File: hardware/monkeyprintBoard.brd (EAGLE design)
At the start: 65 x 55.9 mm, 46 parts, among them Q1 BSS123

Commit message: Updated eagle files.
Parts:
- removed GPIO: (no value), connectors:X10N-DIL
- removed H1, H2, H3, H4: MOUNT-HOLE3.0, holes:3,0
- added ARDUINO_PRO_MICRO: ARDUINOPROMICRO, arduinoProMicro:ARDUINOPROMICRO
- added C7: 100n, rcl:C0603
- added R15: 220R, rcl:R0603
- added R17: 10k, rcl:R0603
- added R19: 0R, rcl:R0603
- added X3: (no value), connectors:X02N-SIL
- U$1: value ARDUINOPROMICRO -> MONKEYPRINTPICONNECTOR; device arduinoProMicro:ARDUINOPROMICRO -> monkeyprintPiConnector:MONKEYPRINTPICONNECTOR
- moved U$1 35.9 mm to (51.6, 3.49)
- moved R8 9.67 mm to (25.4, 48.3), turned to 90 degrees
- moved R10 8.28 mm to (33.0, 48.3), turned to 90 degrees
- moved R12 8.28 mm to (31.1, 48.3), turned to 90 degrees
- moved C4 4.58 mm to (54.0, 9.53)
- moved R5 4.26 mm to (47.0, 31.8), turned to 0 degrees
- moved R2 3.70 mm to (44.5, 31.1)
- moved D1 2.54 mm to (20.3, 52.7)
- moved LEDS 1.91 mm to (61.6, 38.7)
- moved R9 1.42 mm to (48.3, 36.8)
- moved X1 1.35 mm to (18.7, 39.7)
- moved R13 1.27 mm to (59.1, 38.7)
- moved R6 0.90 mm to (53.3, 23.5)
- moved R7 0.90 mm to (55.2, 23.5)
- moved Q1 0.63 mm to (54.0, 20.3)
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- renumbered U$2 to POLOLU_DRV8825_BUILD, U$3 to POLOLU_DRV8825_TILT
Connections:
- new net N$49: R17.1, R19.2, U$6.6
- new net N$50: ARDUINO_PRO_MICRO.14, C7.1, R19.1
- net GND: now also ARDUINO_PRO_MICRO.23, ARDUINO_PRO_MICRO.3, ARDUINO_PRO_MICRO.4, C7.2, U$1.GND1, U$1.GND2, X3.2; no longer GPIO.6, GPIO.9, U$1.23, U$1.3, U$1.4
- net N$1: now also ARDUINO_PRO_MICRO.7; no longer U$1.7
- net N$12: now also ARDUINO_PRO_MICRO.5; no longer U$1.5
- net N$13: now also ARDUINO_PRO_MICRO.6; no longer U$1.6
- net N$2: now also ARDUINO_PRO_MICRO.8; no longer U$1.8
- net N$25: now also ARDUINO_PRO_MICRO.10; no longer U$1.10
- net N$26: now also ARDUINO_PRO_MICRO.1, U$1.RXD; no longer GPIO.10, U$1.1
- net N$27: now also ARDUINO_PRO_MICRO.13; no longer U$1.13
- net N$28: now also ARDUINO_PRO_MICRO.22; no longer U$1.22
- net N$29: now also ARDUINO_PRO_MICRO.16, U$7.4; no longer U$1.16, U$7.1
- net N$31: now also X3.1; no longer U$7.4
- net N$32: now also ARDUINO_PRO_MICRO.19; no longer U$1.19
- net N$33: now also ARDUINO_PRO_MICRO.21; no longer U$1.21
- net N$34: now also ARDUINO_PRO_MICRO.20; no longer U$1.20
- net N$37: now also ARDUINO_PRO_MICRO.2, U$1.TXD; no longer GPIO.8, U$1.2
- net N$38: now also ARDUINO_PRO_MICRO.15, U$7.6; no longer U$1.15, U$7.3
- net N$39: now also ARDUINO_PRO_MICRO.9, U$7.1; no longer U$1.9, U$6.4
- net N$4: now also ARDUINO_PRO_MICRO.12; no longer U$1.12
- net N$41: now also R15.1, U$6.4; no longer U$1.14, U$7.6
- net N$5: now also ARDUINO_PRO_MICRO.18; no longer U$1.18
- net N$6: now also ARDUINO_PRO_MICRO.11; no longer U$1.11
- net N$8: now also ARDUINO_PRO_MICRO.17; no longer U$1.17
- net VCC: now also R15.2, R17.2, U$1.VCC1, U$1.VCC2, U$7.3; no longer GPIO.2, GPIO.4, U$6.6
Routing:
- net N$49: track 0.00 -> 59.8 mm
- net N$31: track 60.8 -> 4.88 mm, vias 2 -> 0
- net N$41: track 49.4 -> 5.75 mm, vias 1 -> 0
- net GND: track 273.5 -> 256.0 mm, vias 6 -> 8
- net N$39: track 26.0 -> 35.9 mm
- net N$8: track 59.6 -> 69.2 mm
- net N$10: track 7.58 -> 1.69 mm
- net N$11: track 5.65 -> 1.69 mm
- net N$38: track 48.7 -> 45.2 mm
- net N$29: track 52.8 -> 49.2 mm
- net N$50: track 0.00 -> 3.54 mm
- net N$14: track 2.85 -> 5.94 mm
- net N$40: track 6.46 -> 3.92 mm
- net V+: track 57.4 -> 54.9 mm
- net VCC: track 175.7 -> 173.8 mm, vias 4 -> 5
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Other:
- board text added: "version 0.91"

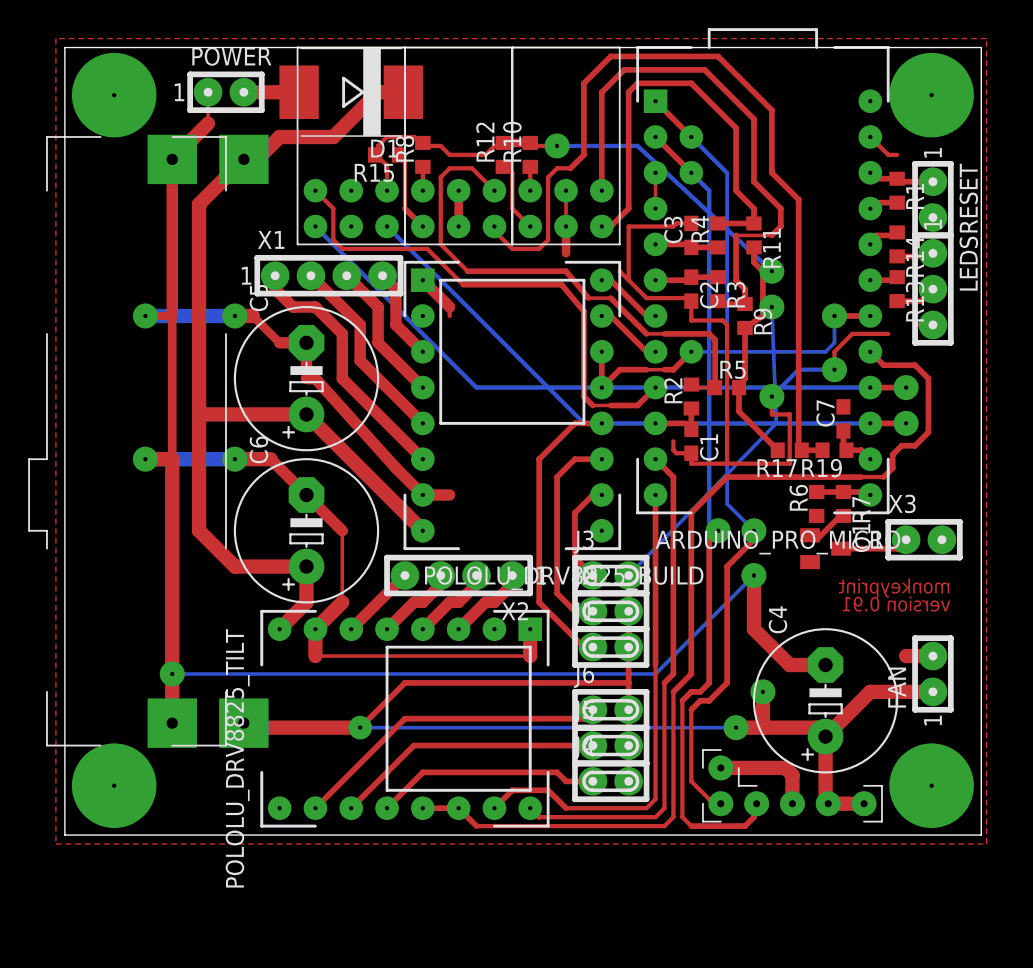
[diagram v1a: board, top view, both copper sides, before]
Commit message: Added compoentent placement guide, minor changes to board.
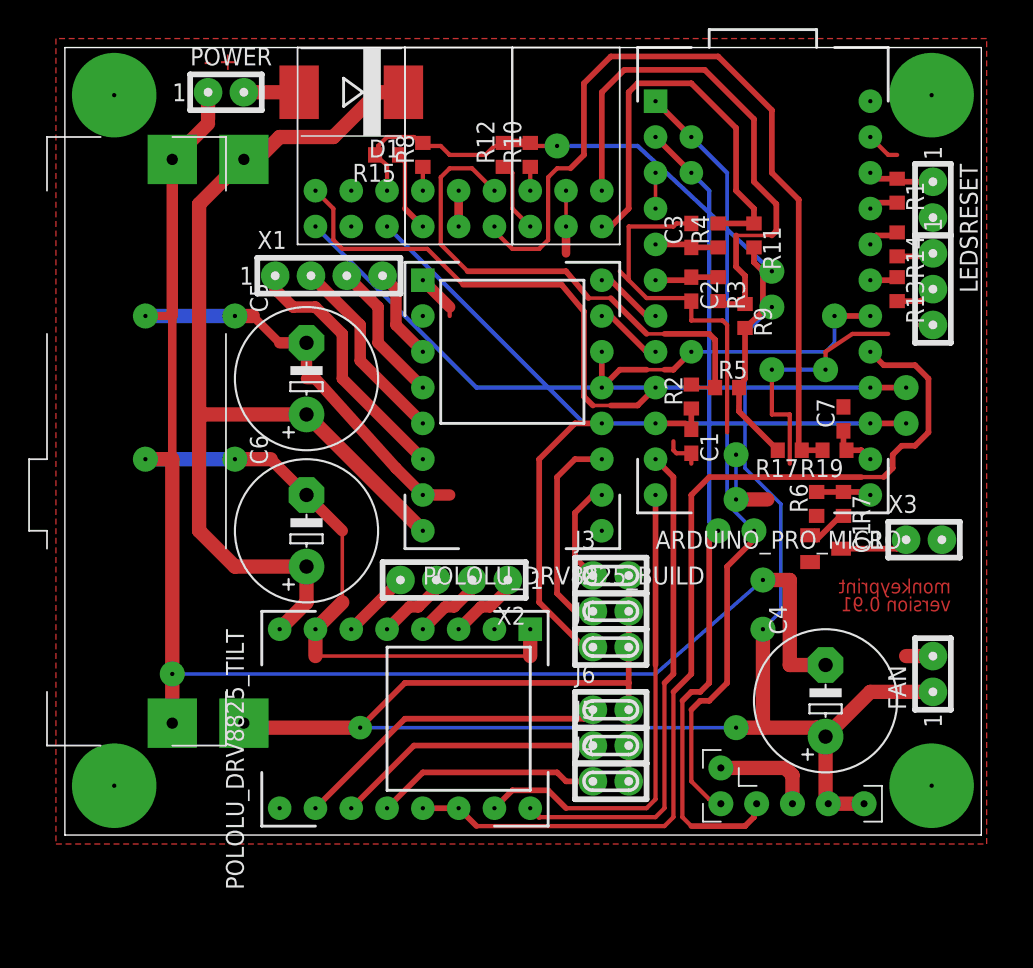
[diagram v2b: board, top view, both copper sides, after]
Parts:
- moved X2 0.45 mm to (27.6, 18.1)
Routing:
- net VCC: track 173.8 -> 180.0 mm, vias 5 -> 6
- net N$8: track 69.2 -> 69.9 mm
- net GND: track 256.0 -> 255.9 mm, vias 8 -> 10
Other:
- board text added: "- +"

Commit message: Published board version 0.92. Fixed shutter servo pinout, swapped gnd and vcc to accomodate most common servo connector pinout.
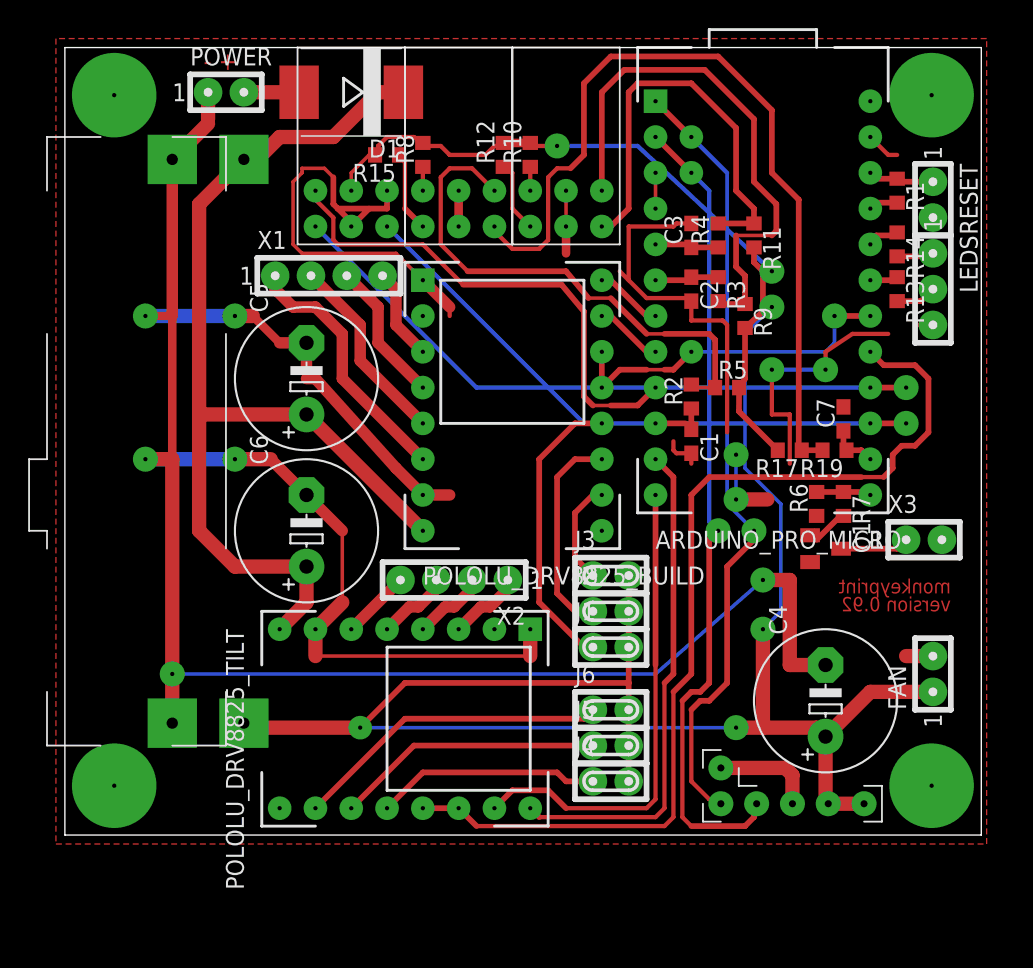
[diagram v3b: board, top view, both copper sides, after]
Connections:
- net GND: now also U$7.3; no longer U$7.2
- net VCC: now also U$7.2; no longer U$7.3
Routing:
- net GND: track 255.9 -> 284.8 mm
- net VCC: track 180.0 -> 180.6 mm
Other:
- board text added: "version 0.92"
- board text removed: "version 0.91"
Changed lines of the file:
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@@
 <layer number="43" name="vRestrict" color="2" fill="10" visible="no" active="yes"/>
 <layer number="44" name="Drills" color="7" fill="1" visible="no" active="yes"/>
-<layer number="45" name="Holes" color="7" fill="1" visible="yes" active="yes"/>
+<layer number="45" name="Holes" color="7" fill="1" visible="no" active="yes"/>
 <layer number="46" name="Milling" color="3" fill="1" visible="no" active="yes"/>
 <layer number="47" name="Measures" color="7" fill="1" visible="no" active="yes"/>
@@
 <text x="55.245" y="15.875" size="1.016" layer="41" ratio="10">version 0.9  </text>
 <text x="62.865" y="17.145" size="1.016" layer="1" ratio="10" rot="MR0">monkeyprint</text>
-<text x="62.865" y="15.875" size="1.016" layer="1" ratio="10" rot="MR0">version 0.91</text>
+<text x="62.865" y="15.875" size="1.016" layer="1" ratio="10" rot="MR0">version 0.92</text>
 <polygon width="0.254" layer="41">
 <vertex x="9.525" y="55.5625"/>
@@
 <vertex x="-0.635" y="56.515"/>
 </polygon>
-<contactref element="U$7" pad="2"/>
 <wire x1="41.275" y1="38.1" x2="40.005" y2="39.37" width="0.3048" layer="1"/>
 <wire x1="40.005" y1="39.37" x2="40.005" y2="43.18" width="0.3048" layer="1"/>
@@
 <wire x1="47.625" y1="23.8125" x2="47.625" y2="26.9875" width="0.254" layer="16"/>
 <wire x1="47.625" y1="23.8125" x2="49.8475" y2="23.8125" width="1.016" layer="1"/>
+<contactref element="U$7" pad="3"/>
+<wire x1="20.32" y1="43.18" x2="20.32" y2="43.4975" width="0.254" layer="1"/>
+<wire x1="20.32" y1="43.4975" x2="19.3675" y2="44.45" width="0.4064" layer="1"/>
+<wire x1="19.3675" y1="44.45" x2="19.05" y2="44.7675" width="0.4064" layer="1"/>
+<wire x1="19.05" y1="44.7675" x2="19.05" y2="46.6725" width="0.4064" layer="1"/>
+<wire x1="19.05" y1="46.6725" x2="18.415" y2="47.3075" width="0.254" layer="1"/>
+<wire x1="18.415" y1="47.3075" x2="16.8275" y2="47.3075" width="0.254" layer="1"/>
+<wire x1="16.8275" y1="47.3075" x2="16.8275" y2="46.99" width="0.254" layer="1"/>
+<wire x1="16.8275" y1="46.99" x2="16.1925" y2="46.355" width="0.254" layer="1"/>
+<wire x1="16.1925" y1="46.355" x2="16.1925" y2="41.91" width="0.254" layer="1"/>
+<wire x1="16.1925" y1="41.91" x2="16.8275" y2="41.275" width="0.254" layer="1"/>
+<wire x1="16.8275" y1="41.275" x2="23.495" y2="41.275" width="0.254" layer="1"/>
+<wire x1="23.495" y1="41.275" x2="25.4" y2="39.37" width="0.254" layer="1"/>
+<wire x1="20.32" y1="43.4975" x2="20.6375" y2="43.4975" width="0.4064" layer="1"/>
+<wire x1="20.6375" y1="43.4975" x2="21.59" y2="44.45" width="0.4064" layer="1"/>
+<wire x1="22.86" y1="44.45" x2="22.86" y2="45.72" width="0.4064" layer="1"/>
+<wire x1="22.86" y1="44.45" x2="19.3675" y2="44.45" width="0.4064" layer="1"/>
 </signal>
 <signal name="V+">
@@
 <wire x1="57.15" y1="10.16" x2="61.595" y2="10.16" width="1.016" layer="1"/>
 <wire x1="54.1655" y1="2.2225" x2="56.7055" y2="2.2225" width="1.016" layer="1"/>
-<contactref element="U$7" pad="3"/>
 <contactref element="R17" pad="2"/>
 <contactref element="R15" pad="2"/>
@@
 <wire x1="22.225" y1="48.895" x2="22.225" y2="48.26" width="0.3048" layer="1"/>
 <wire x1="22.225" y1="48.26" x2="22.01" y2="48.26" width="0.3048" layer="1"/>
-<wire x1="22.01" y1="48.26" x2="22.86" y2="47.5225" width="0.3048" layer="1"/>
-<wire x1="22.86" y1="47.5225" x2="22.86" y2="45.72" width="0.3048" layer="1"/>
 <wire x1="25.4" y1="49.11" x2="25.185" y2="49.11" width="0.3048" layer="1"/>
 <wire x1="25.185" y1="49.11" x2="25.4" y2="48.895" width="0.3048" layer="1"/>
@@
 <via x="49.53" y="14.605" extent="1-16" drill="0.3" diameter="1.778"/>
 <wire x1="49.53" y1="14.605" x2="50.8" y2="15.875" width="0.254" layer="16"/>
+<contactref element="U$7" pad="2"/>
+<wire x1="22.01" y1="48.26" x2="21.59" y2="48.26" width="0.254" layer="1"/>
+<wire x1="21.59" y1="48.26" x2="20.32" y2="46.99" width="0.254" layer="1"/>
+<wire x1="20.32" y1="46.99" x2="20.32" y2="45.72" width="0.254" layer="1"/>
 </signal>
 <signal name="N$25">
@@
 <signal name="N$39">
 <contactref element="ARDUINO_PRO_MICRO" pad="9"/>
-<wire x1="25.7175" y1="41.5925" x2="28.2575" y2="39.0525" width="0.3048" layer="1"/>
+<wire x1="25.4" y1="41.91" x2="28.2575" y2="39.0525" width="0.3048" layer="1"/>
 <wire x1="28.2575" y1="39.0525" x2="35.2425" y2="39.0525" width="0.4064" layer="1"/>
 <wire x1="35.2425" y1="39.0525" x2="36.83" y2="37.1475" width="0.4064" layer="1"/>
@@
 <wire x1="40.64" y1="30.48" x2="41.91" y2="31.75" width="0.4064" layer="1"/>
 <contactref element="U$7" pad="1"/>
-<wire x1="25.7175" y1="41.5925" x2="19.685" y2="41.5925" width="0.3048" layer="1"/>
-<wire x1="19.685" y1="41.5925" x2="19.05" y2="42.2275" width="0.3048" layer="1"/>
-<wire x1="19.05" y1="42.2275" x2="19.05" y2="44.45" width="0.3048" layer="1"/>
-<wire x1="19.05" y1="44.45" x2="17.78" y2="45.72" width="0.3048" layer="1"/>
+<wire x1="25.4" y1="41.91" x2="19.3675" y2="41.91" width="0.3048" layer="1"/>
+<wire x1="19.3675" y1="41.91" x2="19.05" y2="42.2275" width="0.3048" layer="1"/>
+<wire x1="19.05" y1="42.2275" x2="19.05" y2="43.815" width="0.3048" layer="1"/>
+<wire x1="19.05" y1="43.815" x2="17.78" y2="45.085" width="0.3048" layer="1"/>
+<wire x1="17.78" y1="45.085" x2="17.78" y2="45.72" width="0.3048" layer="1"/>
 </signal>
 <signal name="N$40">
